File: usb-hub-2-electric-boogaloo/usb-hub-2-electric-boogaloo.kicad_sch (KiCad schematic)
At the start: 21 parts, among them U1 SL2.1S, U2 GL823K-HCY04

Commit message: probably messed something up, but schema done!
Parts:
- added C11, C13: 10u, symbol Device:C
- added C12, C14, C8: 100n, symbol Device:C
- added R10, R6, R7, R8, R9: 10k, symbol Device:R
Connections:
- net +5V: now also U2.10 (5V), C11.1, C12.1, R6.1, R7.1
- net DM4: now also U2.16 (DM)
- net DP4: now also U2.15 (DP)
- net GND: now also SIM1.10, SIM1.13, SIM1.14, SIM1.6 (VSS), SIM1.9, U2.1 (VSS), U2.14 (VSS), C11.2, C12.2, C13.2, C14.1, C8.2
- net D2: now reaches SIM1.1 (DAT2)
- net D2: now also U2.7 (D2), R8.2
- net D3: now reaches SIM1.2 (CD/DAT3)
- net D3: now also U2.6 (D3), R9.2
- net SD_CMD: now reaches SIM1.3 (CMD)
- net SD_CMD: now also U2.5 (CMD), R10.2
- net SD_VDD: now reaches SIM1.4 (VDD)
- net SD_VDD: now also U2.8 (PMOS), U2.9 (VDD), C13.1, C14.2
- net SD_CLK: now reaches SIM1.5 (CLK)
- net SD_CLK: now also U2.4 (CLK)
- net D0: now reaches SIM1.7 (DAT0)
- net D0: now also U2.3 (D0), R7.2
- net D1: now reaches SIM1.8 (DAT1)
- net D1: now also U2.2 (D1), R6.2
- net at U2.13 (VDDA): now also C8.1
- new net: R10.1, R8.1
- no-connect marks 10 -> 14
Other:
- moved on the sheet: C10, C4, C5, C6, C7, C9, SIM1, U1, U2

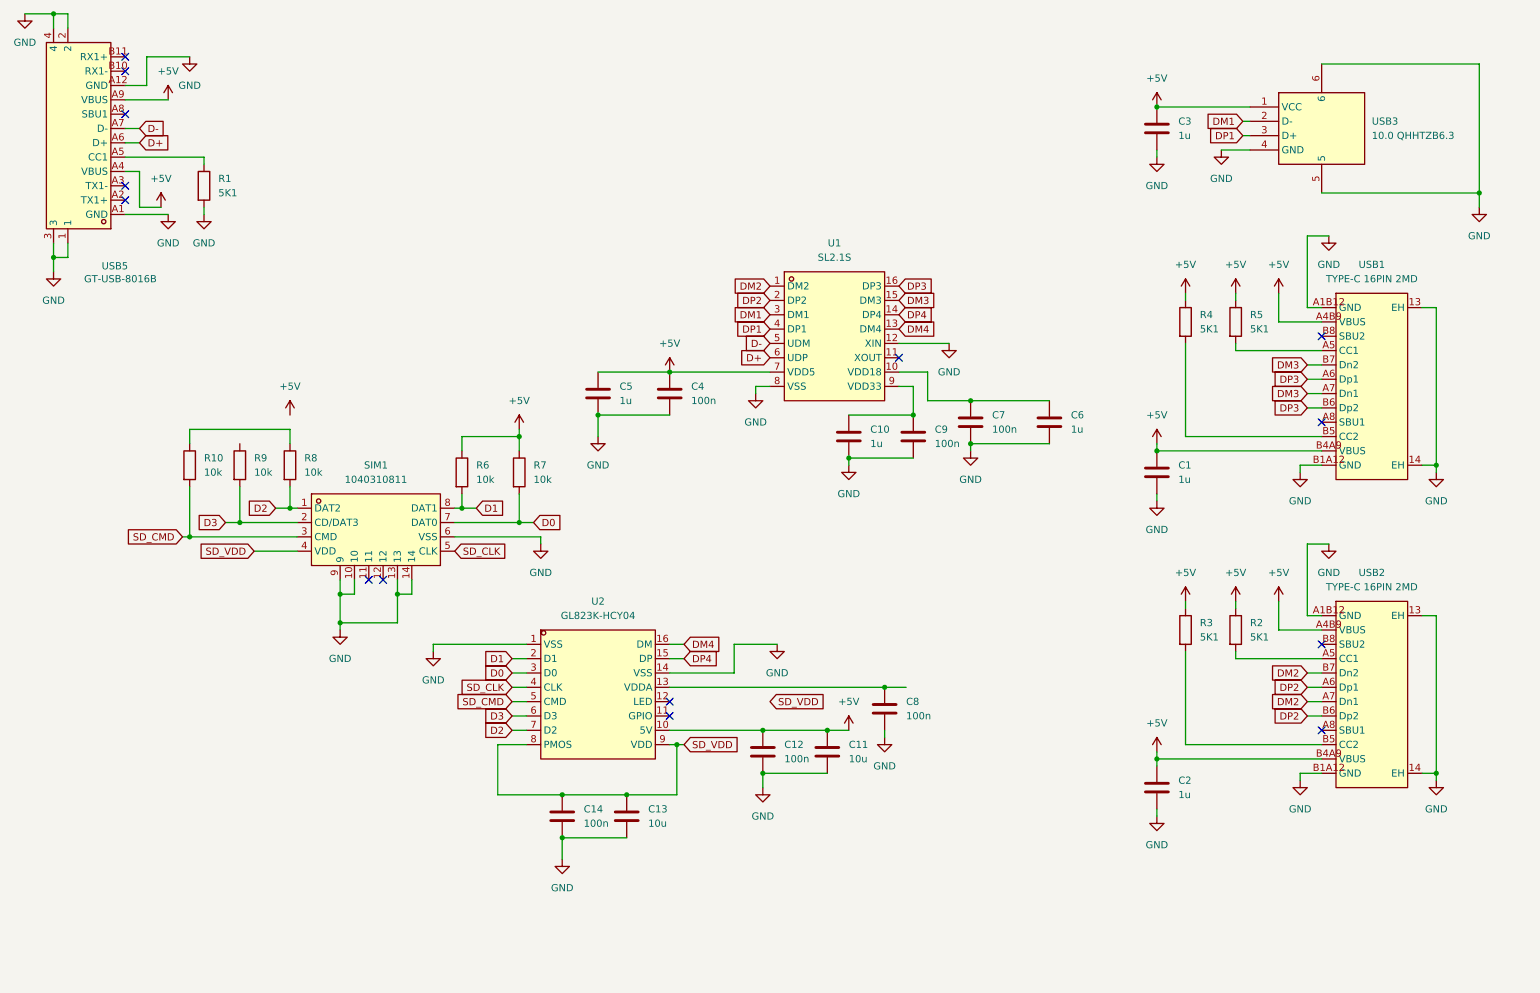
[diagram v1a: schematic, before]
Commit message: fixing schema + lots of esd protection
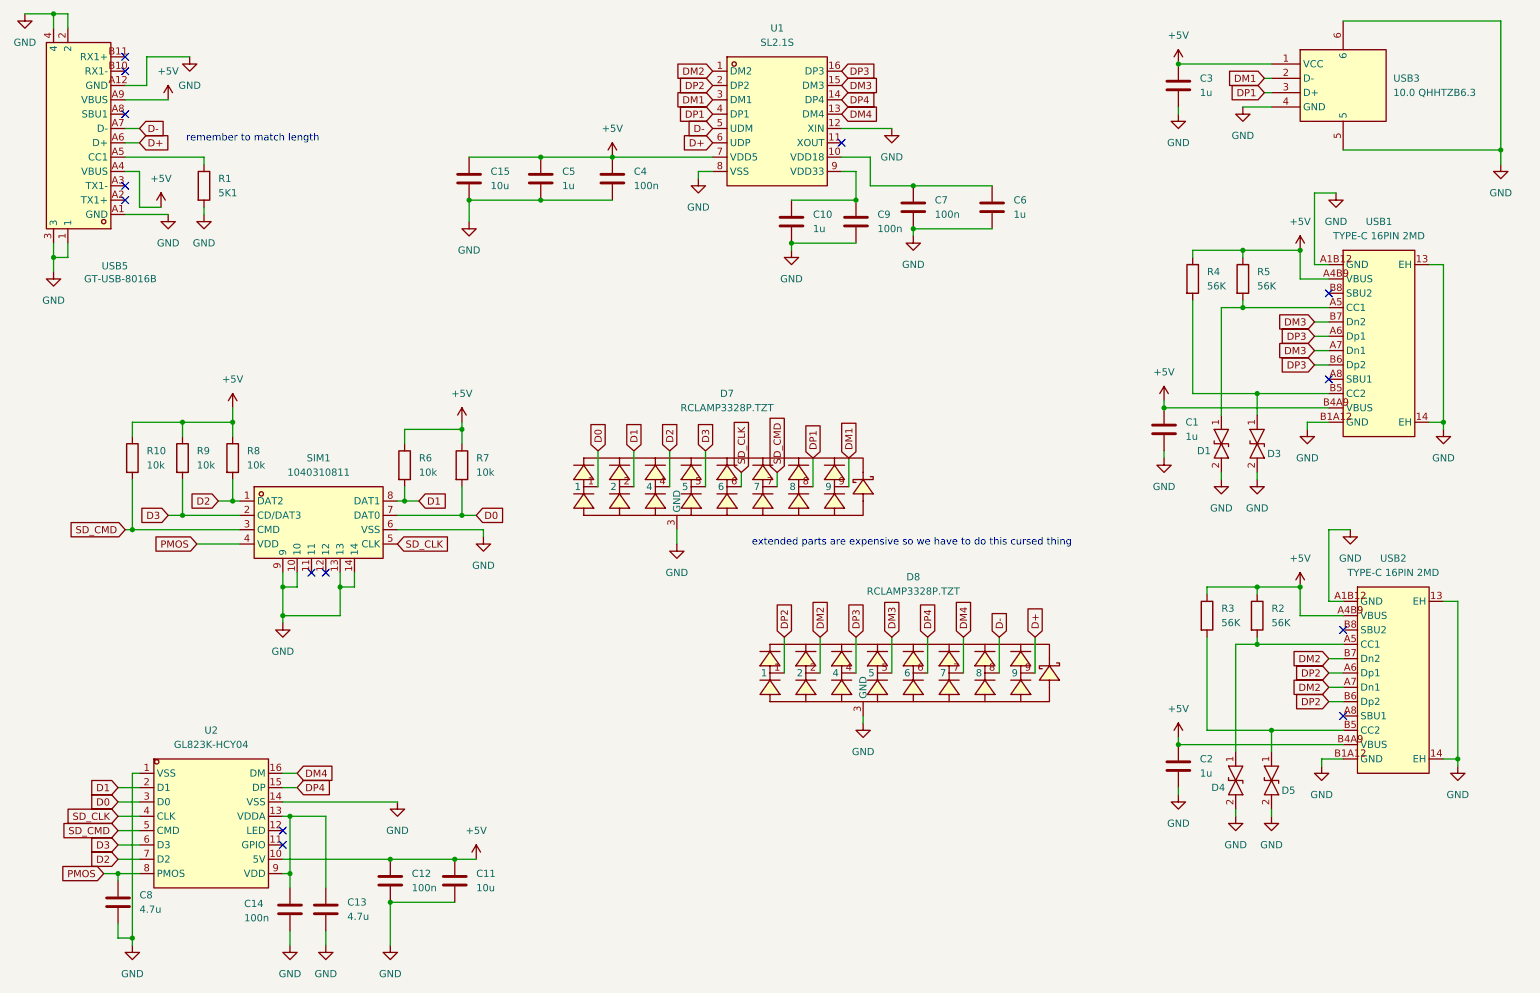
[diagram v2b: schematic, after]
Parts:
- added C15: 10u, symbol Device:C
- added D1, D3, D4, D5: PESD5V0V1BB,115, easyeda2kicad:SOD-523_L1.2-W0.8-LS1.6-RD, symbol easyeda2kicad:PESD5V0V1BB,115
- added D7, D8: RCLAMP3328P.TZT, easyeda2kicad:UDFN-9_L3.9-W1.1-P0.80-BL, symbol easyeda2kicad:RCLAMP3328P.TZT
- C13: value 10u -> 4.7u
- C8: value 100n -> 4.7u
- R2, R3, R4, R5: value 5K1 -> 56K
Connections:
- net +5V: now also R10.1, R8.1, R9.1, C15.1
- net D+: now also D8.9
- net D-: now also D8.8
- net D0: now also D7.1
- net D1: now also D7.2
- net D2: now also D7.4
- net D3: now also D7.5
- net DM1: now also D7.9
- net DM2: now also D8.2
- net DM3: now also D8.5
- net DM4: now also D8.7
- net DP1: now also D7.8
- net DP2: now also D8.1
- net DP3: now also D8.4
- net DP4: now also D8.6
- net GND: now also C15.2, D1.2, D3.2, D4.2, D5.2, D7.3 (GND), D8.3 (GND)
- net SD_CLK: now also D7.6
- net SD_CMD: now also D7.7
- net at R2.2, USB2.A5 (CC1): now also D4.1
- net at R3.2, USB2.B5 (CC2): now also D5.1
- net at R5.2, USB1.A5 (CC1): now also D1.1
- net at R4.2, USB1.B5 (CC2): now also D3.1
- net at U2.13 (VDDA): now also C13.1, C14.2, U2.9 (VDD); no longer C8.1
- removed net SD_VDD: C13.1, C14.2, SIM1.4 (VDD), U2.8 (PMOS), U2.9 (VDD)
- new net PMOS: C8.1, SIM1.4 (VDD), U2.8 (PMOS)
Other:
- note added: "extended parts are expensive so we have to do this cursed thing"
- note added: "remember to match length"
- moved on the sheet: C1, C10, C11, C12, C14, C2, C3, C4, C5, C6, C7, C9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

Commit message: fixed some stuff
schottky + more decoupling caps
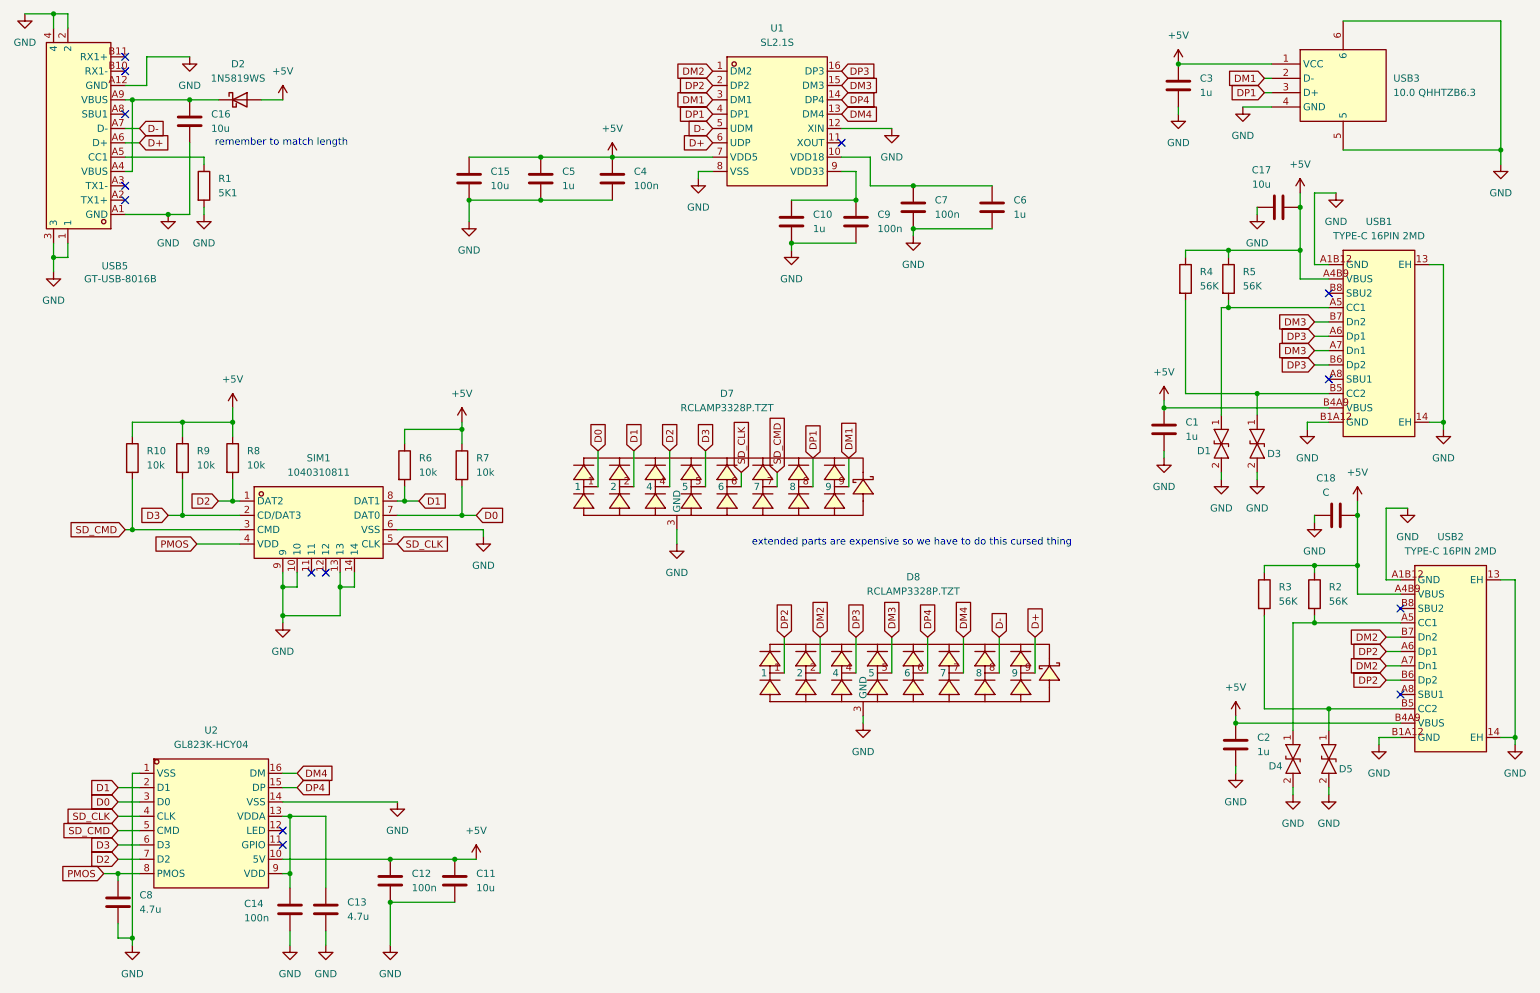
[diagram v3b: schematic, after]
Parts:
- added C16, C17: 10u, symbol Device:C
- added C18: C, symbol Device:C
- added D2: 1N5819WS, Diode_SMD:D_SOD-323, symbol Diode:1N5819WS
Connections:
- net +5V: now also C17.1, C18.2, D2.2 (A); no longer USB5.A4 (VBUS), USB5.A9 (VBUS)
- net GND: now also C16.2, C17.2, C18.1
- new net: C16.1, D2.1 (K), USB5.A4 (VBUS), USB5.A9 (VBUS)
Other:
- moved on the sheet: C2, D4, D5, R2, R3, R4, R5, USB2

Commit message: pcb layout + revise usb-c schema
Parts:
- removed C1, C2: 1u, symbol Device:C
- C10, C11, C12, C13, C14, C15, C16, C17, C3, C4, C5, C6, C7, C8, C9: footprint (none) -> Capacitor_SMD:C_0603_1608Metric_Pad1.08x0.95mm_HandSolder
- C18: value C -> 10u; footprint (none) -> Capacitor_SMD:C_0603_1608Metric_Pad1.08x0.95mm_HandSolder
- R1, R10, R2, R3, R4, R5, R6, R7, R8, R9: footprint (none) -> Resistor_SMD:R_0603_1608Metric_Pad0.98x0.95mm_HandSolder

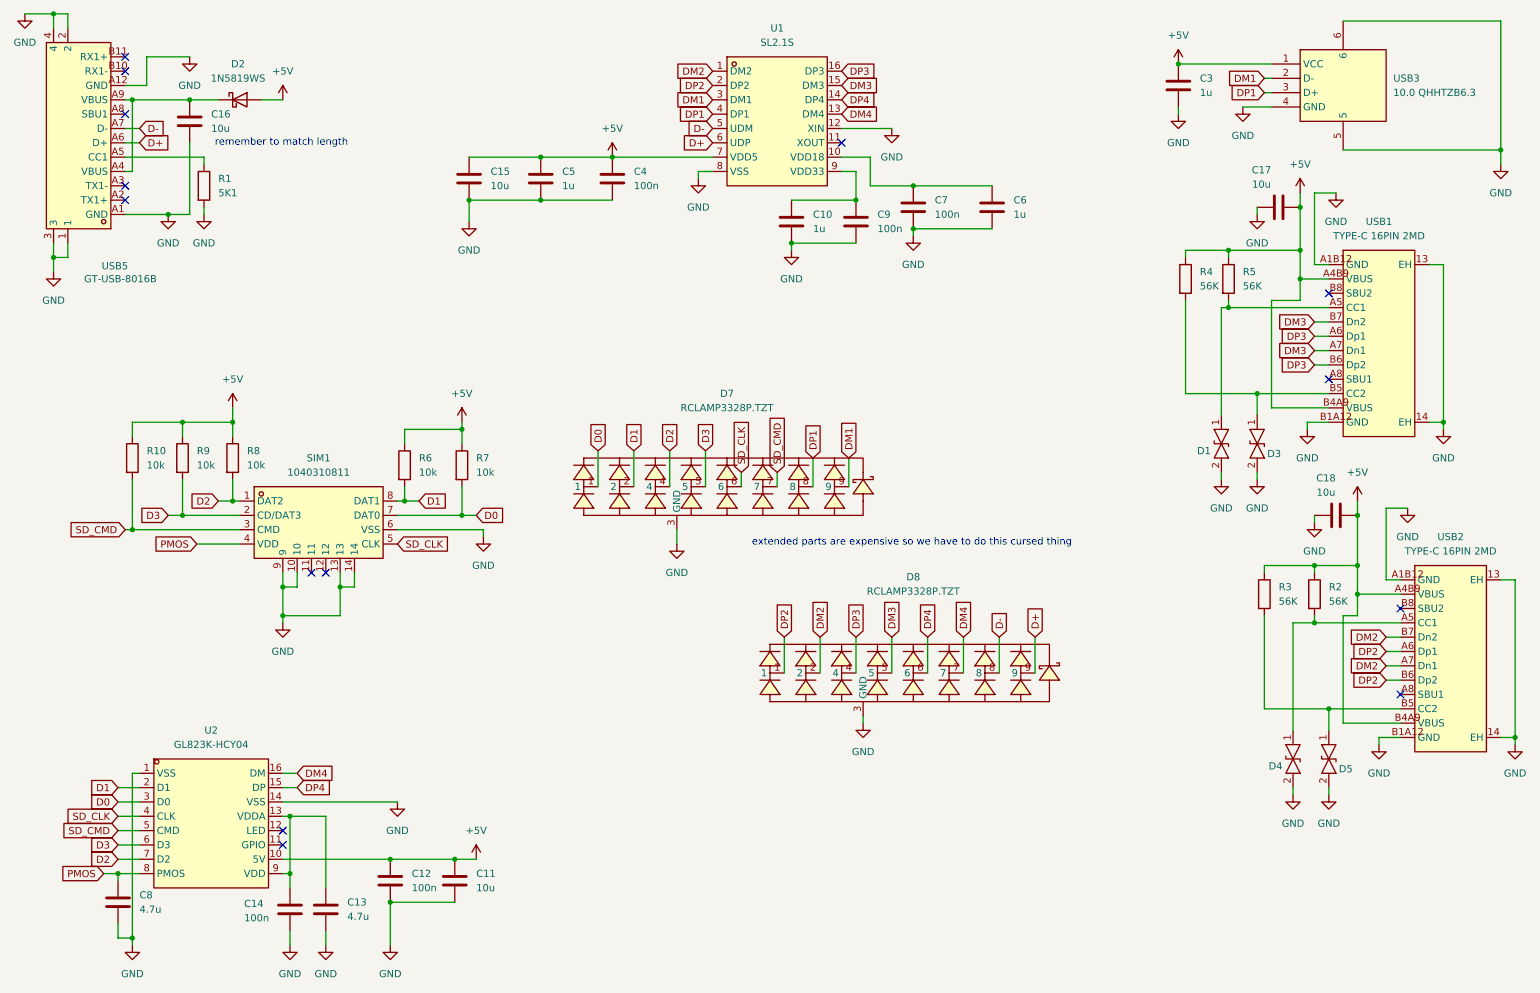
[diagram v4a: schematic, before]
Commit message: routing traces
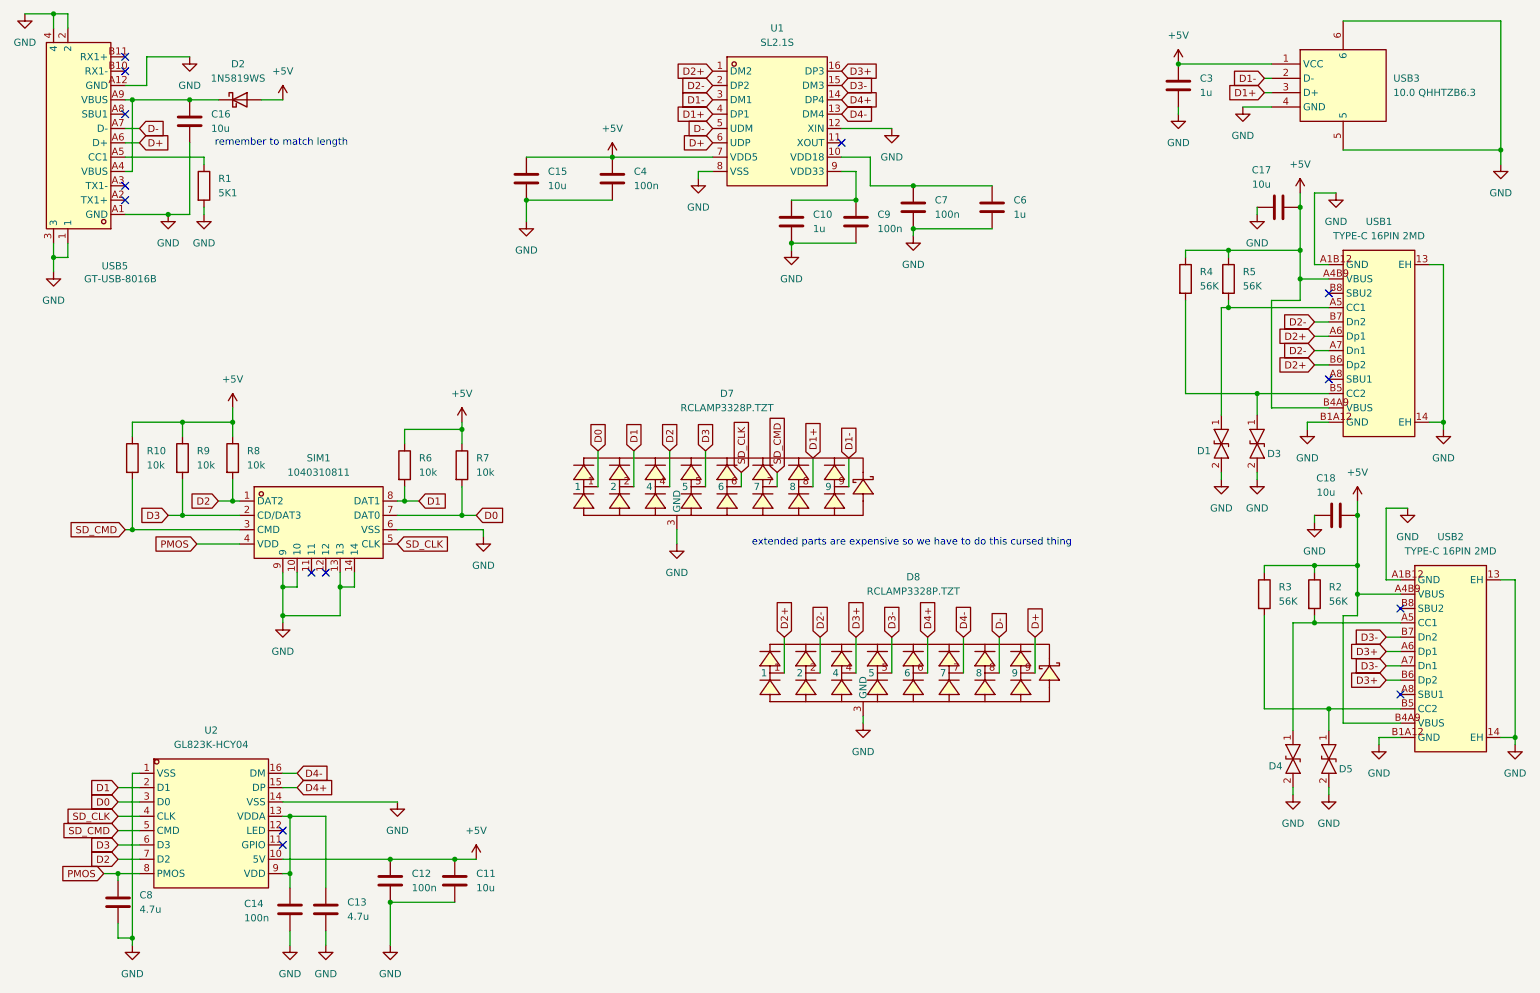
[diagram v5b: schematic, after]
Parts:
- removed C5: 1u, Capacitor_SMD:C_0603_1608Metric_Pad1.08x0.95mm_HandSolder, symbol Device:C
- C10, C15, C4, C6, C7, C9: footprint Capacitor_SMD:C_0603_1608Metric_Pad1.08x0.95mm_HandSolder -> Capacitor_SMD:C_0402_1005Metric_Pad0.74x0.62mm_HandSolder
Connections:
- net DM1 renamed D1-
- net DM2 renamed D3-
- net D3-: now also D8.5, U1.15 (DM3); no longer D8.2, U1.1 (DM2)
- net DM3 renamed D2-
- net D2-: now also D8.2, U1.2 (DP2); no longer D8.5, U1.15 (DM3)
- net DM4 renamed D4-
- net DP1 renamed D1+
- net DP2 renamed D3+
- net D3+: now also D8.4, U1.16 (DP3); no longer D8.1, U1.2 (DP2)
- net DP3 renamed D2+
- net D2+: now also D8.1, U1.1 (DM2); no longer D8.4, U1.16 (DP3)
- net DP4 renamed D4+
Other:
- moved on the sheet: C15
